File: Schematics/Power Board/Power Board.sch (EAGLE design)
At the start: 3 parts

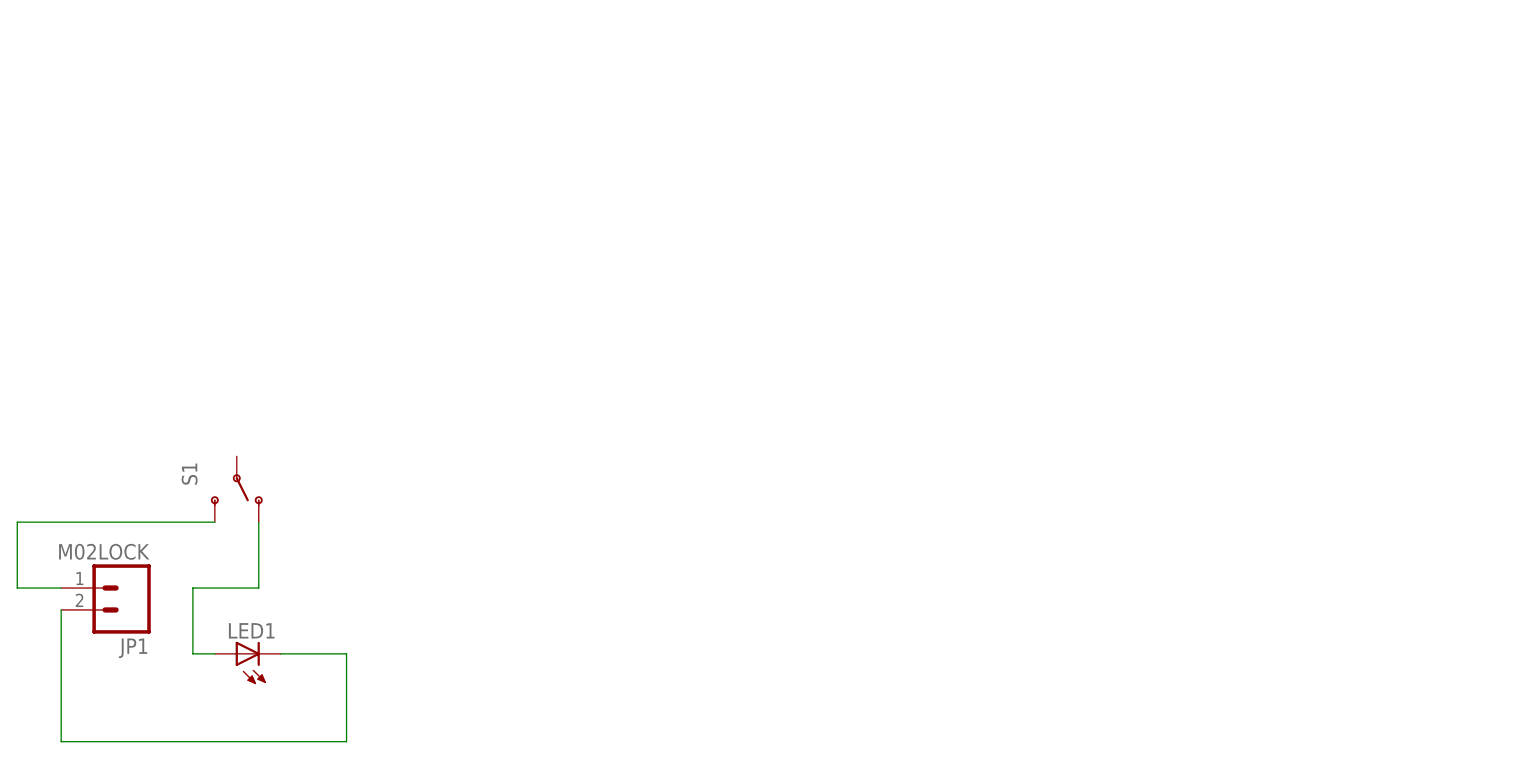
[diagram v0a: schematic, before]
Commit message: Initial power board schematic complete.
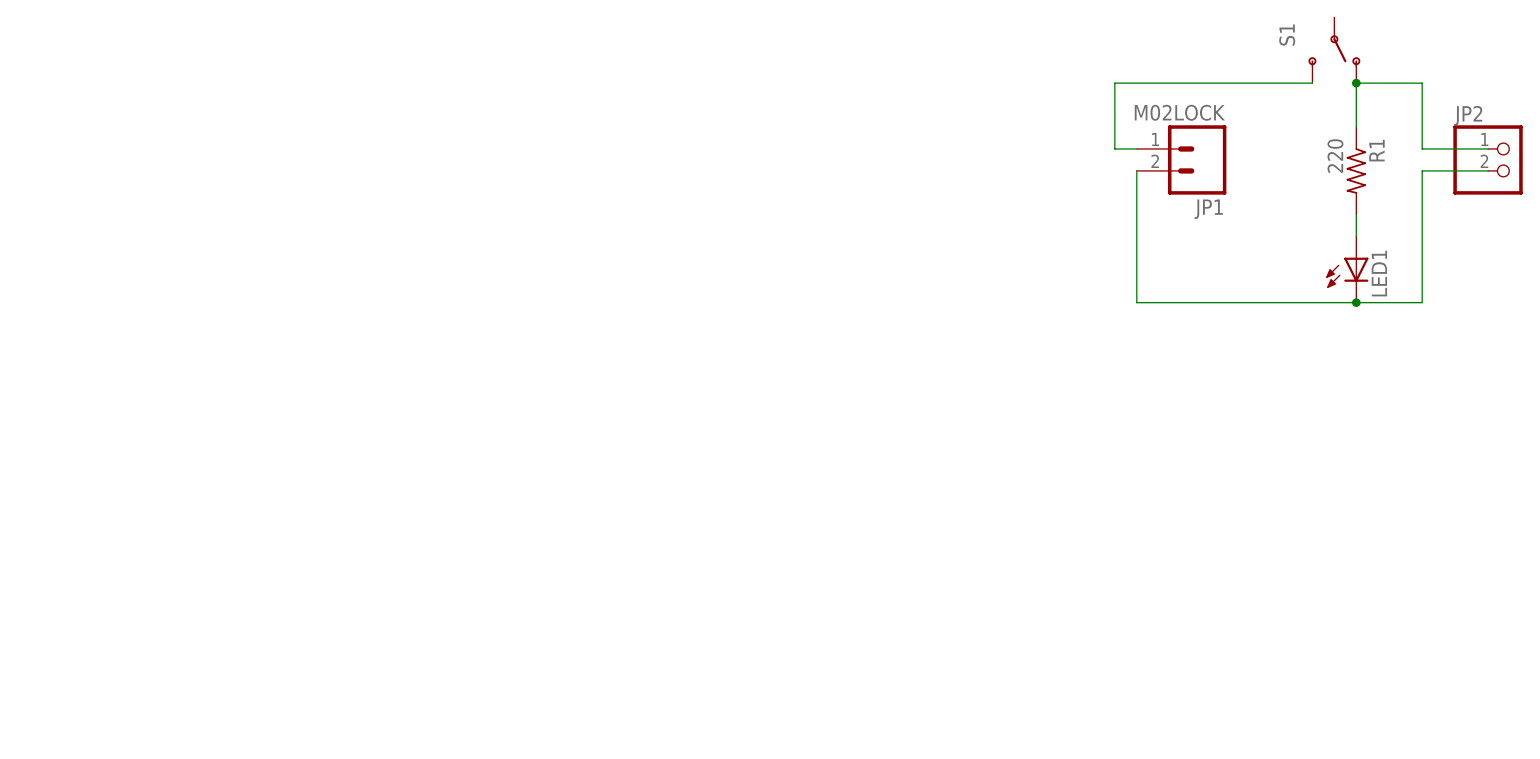
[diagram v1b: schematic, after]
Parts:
- added JP2: (no value), pinhead:PINHD-1X2
- added R1: 220, resistor:R-US_0204/5
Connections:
- new net N$4: JP1.2, JP2.2, LED1.C
- net N$1: now also JP2.1, R1.1, S1.O; no longer JP1.2, LED1.C
- net N$3: now also R1.2; no longer S1.O
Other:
- moved on the sheet: JP1, LED1, S1
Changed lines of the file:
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@@
 <part name="LED1" library="led" deviceset="LED" device="3MM"/>
 <part name="JP1" library="SparkFun-Connectors" deviceset="M02" device="LOCK"/>
+<part name="R1" library="resistor" deviceset="R-US_" device="0204/5" value="220"/>
+<part name="JP2" library="pinhead" deviceset="PINHD-1X2" device=""/>
 </parts>
 <sheets>
@@
 <instance part="FRAME1" gate="G$1" x="0" y="0"/>
 <instance part="FRAME1" gate="G$2" x="172.72" y="0"/>
-<instance part="S1" gate="1" x="38.1" y="86.36" rot="R270"/>
-<instance part="LED1" gate="G$1" x="38.1" y="66.04" rot="R90"/>
-<instance part="JP1" gate="G$1" x="25.4" y="73.66" rot="R180"/>
+<instance part="S1" gate="1" x="165.1" y="137.16" rot="R270"/>
+<instance part="LED1" gate="G$1" x="167.64" y="111.76"/>
+<instance part="JP1" gate="G$1" x="149.86" y="124.46" rot="R180"/>
+<instance part="R1" gate="G$1" x="167.64" y="121.92" rot="R270"/>
+<instance part="JP2" gate="G$1" x="185.42" y="121.92"/>
 </instances>
 <busses>
 </busses>
 <nets>
-<net name="N$1" class="0">
-<segment>
-<pinref part="LED1" gate="G$1" pin="C"/>
-<wire x1="43.18" y1="66.04" x2="50.8" y2="66.04" width="0.1524" layer="91"/>
-<wire x1="50.8" y1="66.04" x2="50.8" y2="55.88" width="0.1524" layer="91"/>
-<pinref part="JP1" gate="G$1" pin="2"/>
-<wire x1="50.8" y1="55.88" x2="17.78" y2="55.88" width="0.1524" layer="91"/>
-<wire x1="17.78" y1="55.88" x2="17.78" y2="71.12" width="0.1524" layer="91"/>
-</segment>
-</net>
 <net name="N$2" class="0">
 <segment>
 <pinref part="JP1" gate="G$1" pin="1"/>
-<wire x1="17.78" y1="73.66" x2="12.7" y2="73.66" width="0.1524" layer="91"/>
-<wire x1="12.7" y1="73.66" x2="12.7" y2="81.28" width="0.1524" layer="91"/>
+<wire x1="142.24" y1="124.46" x2="139.7" y2="124.46" width="0.1524" layer="91"/>
+<wire x1="139.7" y1="124.46" x2="139.7" y2="132.08" width="0.1524" layer="91"/>
 <pinref part="S1" gate="1" pin="S"/>
-<wire x1="12.7" y1="81.28" x2="35.56" y2="81.28" width="0.1524" layer="91"/>
+<wire x1="139.7" y1="132.08" x2="162.56" y2="132.08" width="0.1524" layer="91"/>
+</segment>
+</net>
+<net name="N$1" class="0">
+<segment>
+<pinref part="S1" gate="1" pin="O"/>
+<pinref part="R1" gate="G$1" pin="1"/>
+<wire x1="167.64" y1="132.08" x2="167.64" y2="127" width="0.1524" layer="91"/>
+<wire x1="167.64" y1="132.08" x2="175.26" y2="132.08" width="0.1524" layer="91"/>
+<junction x="167.64" y="132.08"/>
+<wire x1="175.26" y1="132.08" x2="175.26" y2="124.46" width="0.1524" layer="91"/>
+<pinref part="JP2" gate="G$1" pin="1"/>
+<wire x1="175.26" y1="124.46" x2="182.88" y2="124.46" width="0.1524" layer="91"/>
 </segment>
 </net>
 <net name="N$3" class="0">
 <segment>
-<pinref part="S1" gate="1" pin="O"/>
-<wire x1="40.64" y1="81.28" x2="40.64" y2="73.66" width="0.1524" layer="91"/>
-<wire x1="40.64" y1="73.66" x2="33.02" y2="73.66" width="0.1524" layer="91"/>
-<wire x1="33.02" y1="73.66" x2="33.02" y2="66.04" width="0.1524" layer="91"/>
+<pinref part="R1" gate="G$1" pin="2"/>
 <pinref part="LED1" gate="G$1" pin="A"/>
-<wire x1="33.02" y1="66.04" x2="35.56" y2="66.04" width="0.1524" layer="91"/>
+<wire x1="167.64" y1="116.84" x2="167.64" y2="114.3" width="0.1524" layer="91"/>
 </segment>
 </net>
+<net name="N$4" class="0">
+<segment>
+<pinref part="LED1" gate="G$1" pin="C"/>
+<wire x1="167.64" y1="106.68" x2="142.24" y2="106.68" width="0.1524" layer="91"/>
+<wire x1="142.24" y1="106.68" x2="142.24" y2="121.92" width="0.1524" layer="91"/>
+<pinref part="JP1" gate="G$1" pin="2"/>
+<pinref part="JP2" gate="G$1" pin="2"/>
+<wire x1="182.88" y1="121.92" x2="175.26" y2="121.92" width="0.1524" layer="91"/>
+<wire x1="175.26" y1="121.92" x2="175.26" y2="106.68" width="0.1524" layer="91"/>
+<wire x1="175.26" y1="106.68" x2="167.64" y2="106.68" width="0.1524" layer="91"/>
+<junction x="167.64" y="106.68"/>
+</segment>
+</net>
